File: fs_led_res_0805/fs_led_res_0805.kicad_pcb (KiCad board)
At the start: 2 copper layers, 14 x 4 mm, 4 parts

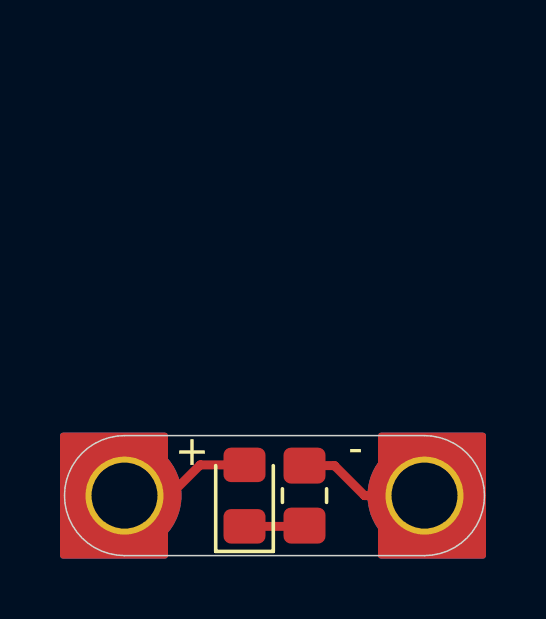
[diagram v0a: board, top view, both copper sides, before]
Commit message: resistor and LED on opposite sides
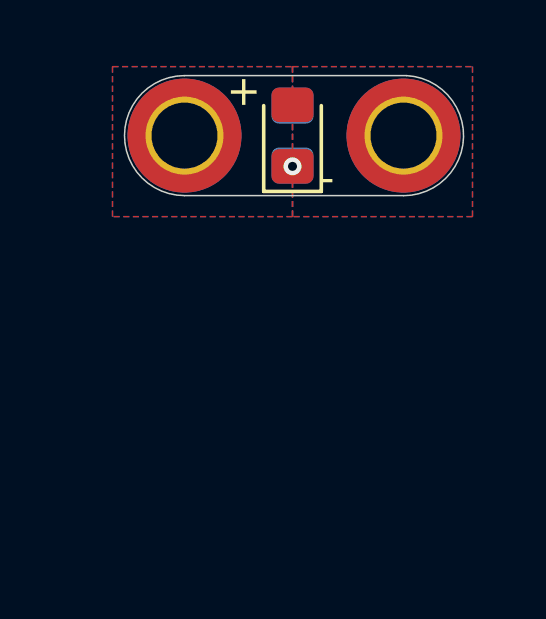
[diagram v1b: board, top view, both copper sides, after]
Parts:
- R1: moved to B.Cu
- moved H1 12.2 mm to (142.0, 68.0), turned to 90 degrees
- moved D1 12.1 mm to (145.6, 68.0)
- moved H2 12.0 mm to (149.3, 68.0)
- moved R1 12.0 mm to (145.6, 68.0)
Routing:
- net VCC: track 4.42 -> 0.00 mm
- net GND: track 4.41 -> 0.00 mm
- net Net-(D1-K): track 2.01 -> 0.00 mm, vias 0 -> 1
- added copper zone on B.Cu, net GND
- added copper zone on F.Cu, net GND
- added copper zone on B.Cu, net VCC
- added copper zone on F.Cu, net VCC
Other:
- board size 14 x 4 mm -> 11.3 x 4 mm
- board text removed: "0805"
- board text removed: "@borisnotes"
